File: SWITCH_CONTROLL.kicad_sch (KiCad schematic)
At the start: 17 parts, among them IC42 ${DEVICE}, IC43 ${DEVICE}, IC44 ${DEVICE}, IC45 ${DEVICE}, IC46 ${DEVICE}

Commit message: Updated schematic and rerouted PCB
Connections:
- net CH_B: now also IC45.6 (ANT2); no longer IC45.10 (RX)
- net DAC_DIR_V1_CH_B: now also IC43.4 (V2); no longer IC43.6 (V1)
- net DAC_DIR_V2_CH_B: now also IC43.6 (V1); no longer IC43.4 (V2)
- net GND: no longer IC45.5 (GND)
- net SW_LPF_IN_CH_B: now also IC45.10 (RX); no longer IC45.6 (ANT2)
- net at C120.1: now also IC43.3 (RF2); no longer IC43.1 (RF1)
- net at C120.2: now also IC45.12 (TX); no longer IC45.4 (ANT1)
- net at C126.1: now also IC43.1 (RF1); no longer IC43.3 (RF2)
- net at C126.2: now also IC45.4 (ANT1); no longer IC45.12 (TX)
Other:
- moved on the sheet: IC43

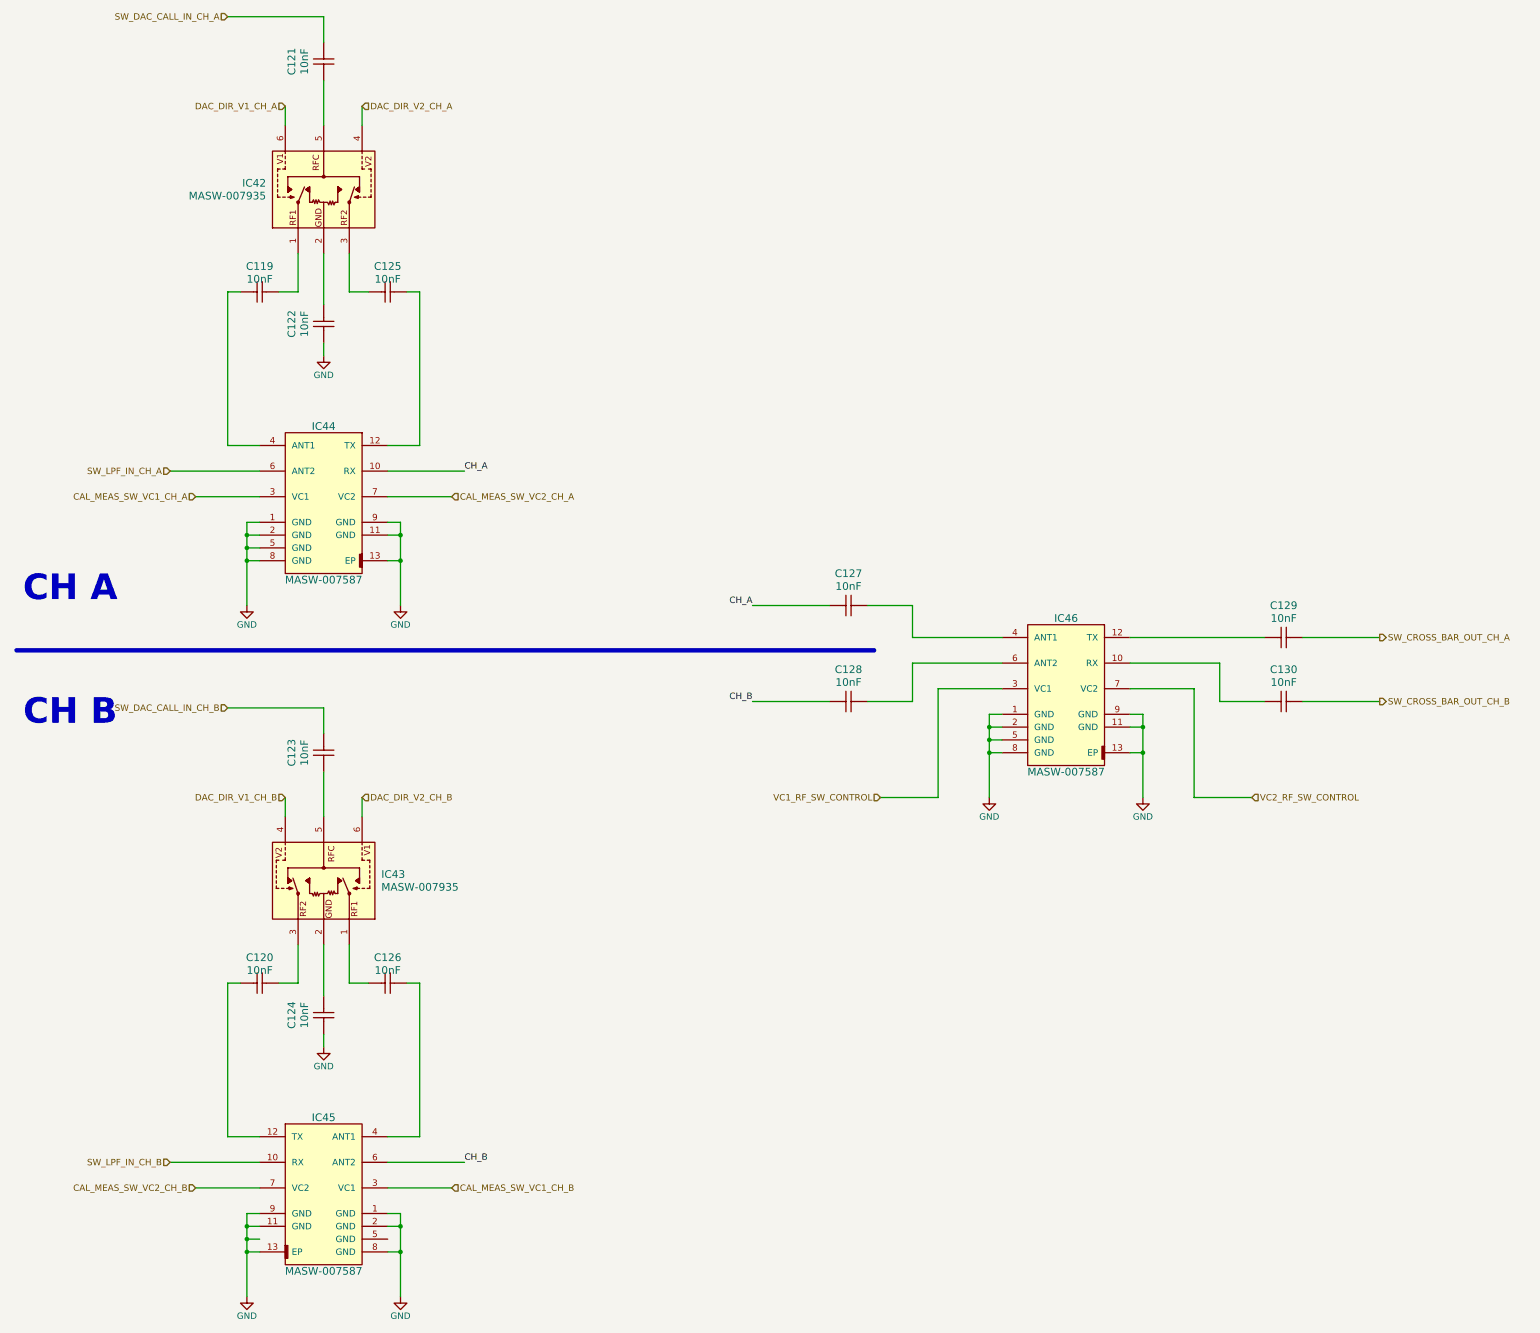
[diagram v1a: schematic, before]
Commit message: Rerouted PCB Logic part
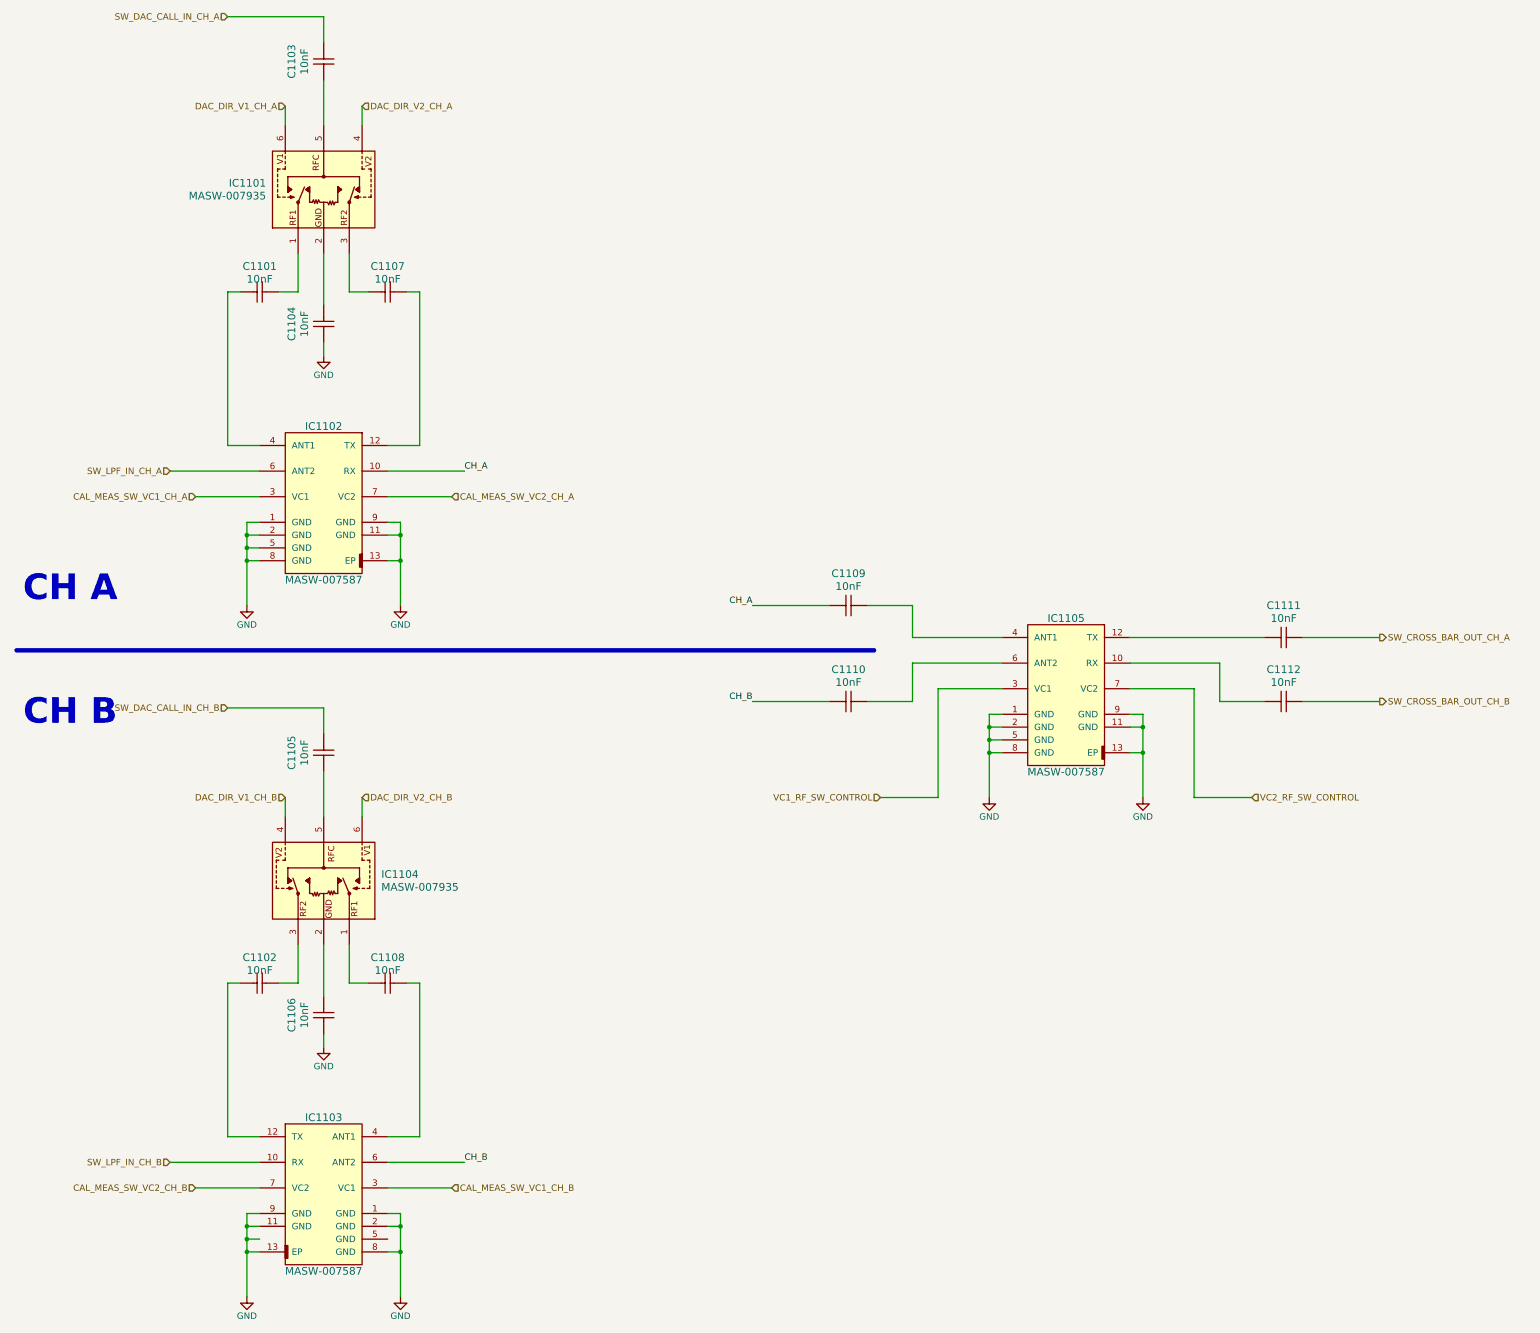
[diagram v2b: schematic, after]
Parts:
- renumbered C119 to C1101, C120 to C1102, C121 to C1103, C122 to C1104, C123 to C1105, C124 to C1106, C125 to C1107, C126 to C1108, C127 to C1109, C128 to C1110, C129 to C1111, C130 to C1112, IC42 to IC1101, IC44 to IC1102, IC45 to IC1103, IC43 to IC1104, IC46 to IC1105
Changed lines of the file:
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@@
 		(dnp no)
 		(fields_autoplaced yes)
-		(property "Reference" "C125"
+		(property "Reference" "C1107"
 			(at 96.52 71.12 0)
 			(effects
@@
 			(project "8CH_Analog_Front_END"
 				(path "/41597329-5145-432a-9041-5bc2cec82d9b/e0337a1b-c397-4f99-b607-786eab07764a/a07ff87c-bda9-449e-8493-adc70ab92011"
-					(reference "C125")
+					(reference "C1107")
 					(unit 1)
 				)
@@
 		(on_board yes)
 		(dnp no)
-		(property "Reference" "#PWR0219"
+		(property "Reference" "#PWR01103"
 			(at 83.82 95.25 0)
 			(effects
@@
 			(project "8CH_Analog_Front_END"
 				(path "/41597329-5145-432a-9041-5bc2cec82d9b/e0337a1b-c397-4f99-b607-786eab07764a/a07ff87c-bda9-449e-8493-adc70ab92011"
-					(reference "#PWR0219")
+					(reference "#PWR01103")
 					(unit 1)
 				)
@@
 		(dnp no)
 		(fields_autoplaced yes)
-		(property "Reference" "C128"
+		(property "Reference" "C1110"
 			(at 187.96 151.13 0)
 			(effects
@@
 			(project "8CH_Analog_Front_END"
 				(path "/41597329-5145-432a-9041-5bc2cec82d9b/e0337a1b-c397-4f99-b607-786eab07764a/a07ff87c-bda9-449e-8493-adc70ab92011"
-					(reference "C128")
+					(reference "C1110")
 					(unit 1)
 				)
@@
 		(dnp no)
 		(fields_autoplaced yes)
-		(property "Reference" "C121"
+		(property "Reference" "C1103"
 			(at 77.47 30.48 0)
 			(effects
@@
 			(project "8CH_Analog_Front_END"
 				(path "/41597329-5145-432a-9041-5bc2cec82d9b/e0337a1b-c397-4f99-b607-786eab07764a/a07ff87c-bda9-449e-8493-adc70ab92011"
-					(reference "C121")
+					(reference "C1103")
 					(unit 1)
 				)
@@
 		(dnp no)
 		(fields_autoplaced yes)
-		(property "Reference" "C123"
+		(property "Reference" "C1105"
 			(at 77.47 167.64 0)
 			(effects
@@
 			(project "8CH_Analog_Front_END"
 				(path "/41597329-5145-432a-9041-5bc2cec82d9b/e0337a1b-c397-4f99-b607-786eab07764a/a07ff87c-bda9-449e-8493-adc70ab92011"
-					(reference "C123")
+					(reference "C1105")
 					(unit 1)
 				)
@@
 		(on_board yes)
 		(dnp no)
-		(property "Reference" "#PWR0215"
+		(property "Reference" "#PWR01101"
 			(at 68.58 144.78 0)
 			(effects
@@
 			(project "8CH_Analog_Front_END"
 				(path "/41597329-5145-432a-9041-5bc2cec82d9b/e0337a1b-c397-4f99-b607-786eab07764a/a07ff87c-bda9-449e-8493-adc70ab92011"
-					(reference "#PWR0215")
+					(reference "#PWR01101")
 					(unit 1)
 				)
@@
 		(dnp no)
 		(fields_autoplaced yes)
-		(property "Reference" "C124"
+		(property "Reference" "C1106"
 			(at 77.47 219.71 0)
 			(effects
@@
 			(project "8CH_Analog_Front_END"
 				(path "/41597329-5145-432a-9041-5bc2cec82d9b/e0337a1b-c397-4f99-b607-786eab07764a/a07ff87c-bda9-449e-8493-adc70ab92011"
-					(reference "C124")
+					(reference "C1106")
 					(unit 1)
 				)
@@
 		(dnp no)
 		(fields_autoplaced yes)
-		(property "Reference" "C119"
+		(property "Reference" "C1101"
 			(at 71.12 71.12 0)
 			(effects
@@
 			(project "8CH_Analog_Front_END"
 				(path "/41597329-5145-432a-9041-5bc2cec82d9b/e0337a1b-c397-4f99-b607-786eab07764a/a07ff87c-bda9-449e-8493-adc70ab92011"
-					(reference "C119")
+					(reference "C1101")
 					(unit 1)
 				)
@@
 		(on_board yes)
 		(dnp no)
-		(property "Reference" "#PWR0220"
+		(property "Reference" "#PWR01102"
 			(at 68.58 281.94 0)
 			(effects
@@
 			(project "8CH_Analog_Front_END"
 				(path "/41597329-5145-432a-9041-5bc2cec82d9b/e0337a1b-c397-4f99-b607-786eab07764a/a07ff87c-bda9-449e-8493-adc70ab92011"
-					(reference "#PWR0220")
+					(reference "#PWR01102")
 					(unit 1)
 				)
@@
 		(dnp no)
 		(fields_autoplaced yes)
-		(property "Reference" "C120"
+		(property "Reference" "C1102"
 			(at 71.12 208.28 0)
 			(effects
@@
 			(project "8CH_Analog_Front_END"
 				(path "/41597329-5145-432a-9041-5bc2cec82d9b/e0337a1b-c397-4f99-b607-786eab07764a/a07ff87c-bda9-449e-8493-adc70ab92011"
-					(reference "C120")
+					(reference "C1102")
 					(unit 1)
 				)
@@
 		(on_board yes)
 		(dnp no)
-		(property "Reference" "#PWR0217"
+		(property "Reference" "#PWR01107"
 			(at 215.9 182.88 0)
 			(effects
@@
 			(project "8CH_Analog_Front_END"
 				(path "/41597329-5145-432a-9041-5bc2cec82d9b/e0337a1b-c397-4f99-b607-786eab07764a/a07ff87c-bda9-449e-8493-adc70ab92011"
-					(reference "#PWR0217")
+					(reference "#PWR01107")
 					(unit 1)
 				)
@@
 		(dnp no)
 		(fields_autoplaced yes)
-		(property "Reference" "C127"
+		(property "Reference" "C1109"
 			(at 187.96 132.08 0)
 			(effects
@@
 			(project "8CH_Analog_Front_END"
 				(path "/41597329-5145-432a-9041-5bc2cec82d9b/e0337a1b-c397-4f99-b607-786eab07764a/a07ff87c-bda9-449e-8493-adc70ab92011"
-					(reference "C127")
+					(reference "C1109")
 					(unit 1)
 				)
@@
 		(on_board yes)
 		(dnp no)
-		(property "Reference" "IC42"
+		(property "Reference" "IC1101"
 			(at 72.39 54.6099 90)
 			(effects
@@
 			(project "8CH_Analog_Front_END"
 				(path "/41597329-5145-432a-9041-5bc2cec82d9b/e0337a1b-c397-4f99-b607-786eab07764a/a07ff87c-bda9-449e-8493-adc70ab92011"
-					(reference "IC42")
+					(reference "IC1101")
 					(unit 1)
 				)
@@
 		(on_board yes)
 		(dnp no)
-		(property "Reference" "IC46"
+		(property "Reference" "IC1105"
 			(at 231.14 140.97 0)
 			(effects
@@
 			(project "8CH_Analog_Front_END"
 				(path "/41597329-5145-432a-9041-5bc2cec82d9b/e0337a1b-c397-4f99-b607-786eab07764a/a07ff87c-bda9-449e-8493-adc70ab92011"
-					(reference "IC46")
+					(reference "IC1105")
 					(unit 1)
 				)
@@
 		(on_board yes)
 		(dnp no)
-		(property "Reference" "#PWR0221"
+		(property "Reference" "#PWR01106"
 			(at 99.06 281.94 0)
 			(effects
@@
 			(project "8CH_Analog_Front_END"
 				(path "/41597329-5145-432a-9041-5bc2cec82d9b/e0337a1b-c397-4f99-b607-786eab07764a/a07ff87c-bda9-449e-8493-adc70ab92011"
-					(reference "#PWR0221")
+					(reference "#PWR01106")
 					(unit 1)
 				)
@@
 		(on_board yes)
 		(dnp no)
-		(property "Reference" "IC43"
+		(property "Reference" "IC1104"
 			(at 95.25 191.7699 90)
 			(effects
@@
 			(project "8CH_Analog_Front_END"
 				(path "/41597329-5145-432a-9041-5bc2cec82d9b/e0337a1b-c397-4f99-b607-786eab07764a/a07ff87c-bda9-449e-8493-adc70ab92011"
-					(reference "IC43")
+					(reference "IC1104")
 					(unit 1)
 				)
@@
 		(dnp no)
 		(fields_autoplaced yes)
-		(property "Reference" "C122"
+		(property "Reference" "C1104"
 			(at 77.47 82.55 0)
 			(effects
@@
 			(project "8CH_Analog_Front_END"
 				(path "/41597329-5145-432a-9041-5bc2cec82d9b/e0337a1b-c397-4f99-b607-786eab07764a/a07ff87c-bda9-449e-8493-adc70ab92011"
-					(reference "C122")
+					(reference "C1104")
 					(unit 1)
 				)
@@
 		(on_board yes)
 		(dnp no)
-		(property "Reference" "IC44"
+		(property "Reference" "IC1102"
 			(at 83.82 102.87 0)
 			(effects
@@
 			(project "8CH_Analog_Front_END"
 				(path "/41597329-5145-432a-9041-5bc2cec82d9b/e0337a1b-c397-4f99-b607-786eab07764a/a07ff87c-bda9-449e-8493-adc70ab92011"
-					(reference "IC44")
+					(reference "IC1102")
 					(unit 1)
 				)
@@
 		(dnp no)
 		(fields_autoplaced yes)
-		(property "Reference" "C130"
+		(property "Reference" "C1112"
 			(at 274.32 151.13 0)
 			(effects
@@
 			(project "8CH_Analog_Front_END"
 				(path "/41597329-5145-432a-9041-5bc2cec82d9b/e0337a1b-c397-4f99-b607-786eab07764a/a07ff87c-bda9-449e-8493-adc70ab92011"
-					(reference "C130")
+					(reference "C1112")
 					(unit 1)
 				)
@@
 		(on_board yes)
 		(dnp no)
-		(property "Reference" "IC45"
+		(property "Reference" "IC1103"
 			(at 83.82 240.03 0)
 			(effects
@@
 			(project "8CH_Analog_Front_END"
 				(path "/41597329-5145-432a-9041-5bc2cec82d9b/e0337a1b-c397-4f99-b607-786eab07764a/a07ff87c-bda9-449e-8493-adc70ab92011"
-					(reference "IC45")
+					(reference "IC1103")
 					(unit 1)
 				)
@@
 		(on_board yes)
 		(dnp no)
-		(property "Reference" "#PWR0216"
+		(property "Reference" "#PWR01105"
 			(at 99.06 144.78 0)
 			(effects
@@
 			(project "8CH_Analog_Front_END"
 				(path "/41597329-5145-432a-9041-5bc2cec82d9b/e0337a1b-c397-4f99-b607-786eab07764a/a07ff87c-bda9-449e-8493-adc70ab92011"
-					(reference "#PWR0216")
+					(reference "#PWR01105")
 					(unit 1)
 				)
@@
 		(on_board yes)
 		(dnp no)
-		(property "Reference" "#PWR0214"
+		(property "Reference" "#PWR01108"
 			(at 246.38 182.88 0)
 			(effects
@@
 			(project "8CH_Analog_Front_END"
 				(path "/41597329-5145-432a-9041-5bc2cec82d9b/e0337a1b-c397-4f99-b607-786eab07764a/a07ff87c-bda9-449e-8493-adc70ab92011"
-					(reference "#PWR0214")
+					(reference "#PWR01108")
 					(unit 1)
 				)
@@
 		(on_board yes)
 		(dnp no)
-		(property "Reference" "#PWR0218"
+		(property "Reference" "#PWR01104"
 			(at 83.82 232.41 0)
 			(effects
@@
 			(project "8CH_Analog_Front_END"
 				(path "/41597329-5145-432a-9041-5bc2cec82d9b/e0337a1b-c397-4f99-b607-786eab07764a/a07ff87c-bda9-449e-8493-adc70ab92011"
-					(reference "#PWR0218")
+					(reference "#PWR01104")
 					(unit 1)
 				)
@@
 		(dnp no)
 		(fields_autoplaced yes)
-		(property "Reference" "C129"
+		(property "Reference" "C1111"
 			(at 274.32 138.43 0)
 			(effects
@@
 			(project "8CH_Analog_Front_END"
 				(path "/41597329-5145-432a-9041-5bc2cec82d9b/e0337a1b-c397-4f99-b607-786eab07764a/a07ff87c-bda9-449e-8493-adc70ab92011"
-					(reference "C129")
+					(reference "C1111")
 					(unit 1)
 				)
@@
 		(dnp no)
 		(fields_autoplaced yes)
-		(property "Reference" "C126"
+		(property "Reference" "C1108"
 			(at 96.52 208.28 0)
 			(effects
@@
 			(project "8CH_Analog_Front_END"
 				(path "/41597329-5145-432a-9041-5bc2cec82d9b/e0337a1b-c397-4f99-b607-786eab07764a/a07ff87c-bda9-449e-8493-adc70ab92011"
-					(reference "C126")
+					(reference "C1108")
 					(unit 1)
 				)

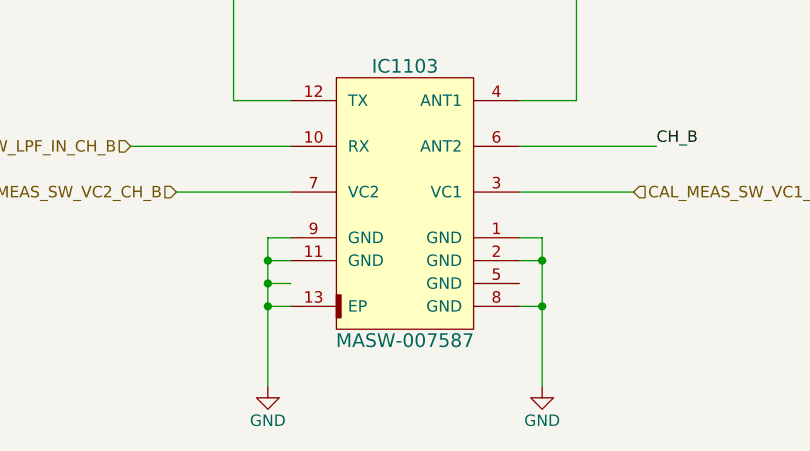
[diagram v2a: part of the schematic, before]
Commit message: GND Vias added
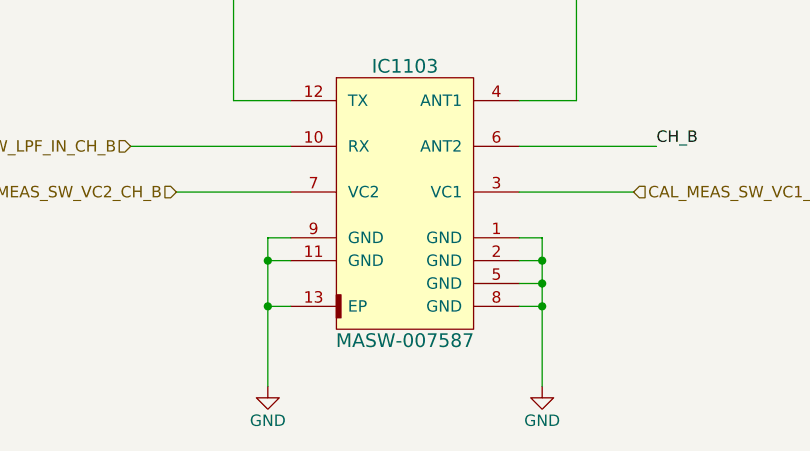
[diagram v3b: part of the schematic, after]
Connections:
- net GND: now also IC1103.5 (GND)
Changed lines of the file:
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@@
 	)
 	(junction
-		(at 68.58 264.16)
+		(at 99.06 264.16)
 		(diameter 0)
 		(color 0 0 0 0)
@@
 	(wire
 		(pts
-			(xy 68.58 264.16) (xy 68.58 266.7)
+			(xy 68.58 261.62) (xy 68.58 266.7)
 		)
 		(stroke
@@
 	(wire
 		(pts
-			(xy 68.58 261.62) (xy 68.58 264.16)
-		)
-		(stroke
-			(width 0)
-			(type default)
-		)
-	)
-	(wire
-		(pts
 			(xy 91.44 39.37) (xy 91.44 43.18)
 		)
@@
 	(wire
 		(pts
-			(xy 99.06 261.62) (xy 99.06 266.7)
+			(xy 99.06 261.62) (xy 99.06 264.16)
 		)
 		(stroke
@@
 	(wire
 		(pts
+			(xy 96.52 264.16) (xy 99.06 264.16)
+		)
+		(stroke
+			(width 0)
+			(type default)
+		)
+	)
+	(wire
+		(pts
 			(xy 200.66 157.48) (xy 200.66 149.86)
 		)
@@
 		(pts
 			(xy 83.82 171.45) (xy 83.82 180.34)
-		)
-		(stroke
-			(width 0)
-			(type default)
-		)
-	)
-	(wire
-		(pts
-			(xy 71.12 264.16) (xy 68.58 264.16)
 		)
 		(stroke
@@
 		)
 		(stroke
+			(width 0)
+			(type default)
+		)
+	)
+	(wire
+		(pts
+			(xy 99.06 264.16) (xy 99.06 266.7)
+		)
+		(stroke
